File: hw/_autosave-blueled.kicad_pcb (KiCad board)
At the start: 2 copper layers, 24.1 x 54.6 mm, 18 parts, among them J1 Barrel_Jack, J2 Screw_Terminal_01x03, J3 ICSP, U1 ATmega328P-AU, U3 LM1117-3.3, X1 RESON-MURATA-CSTCE

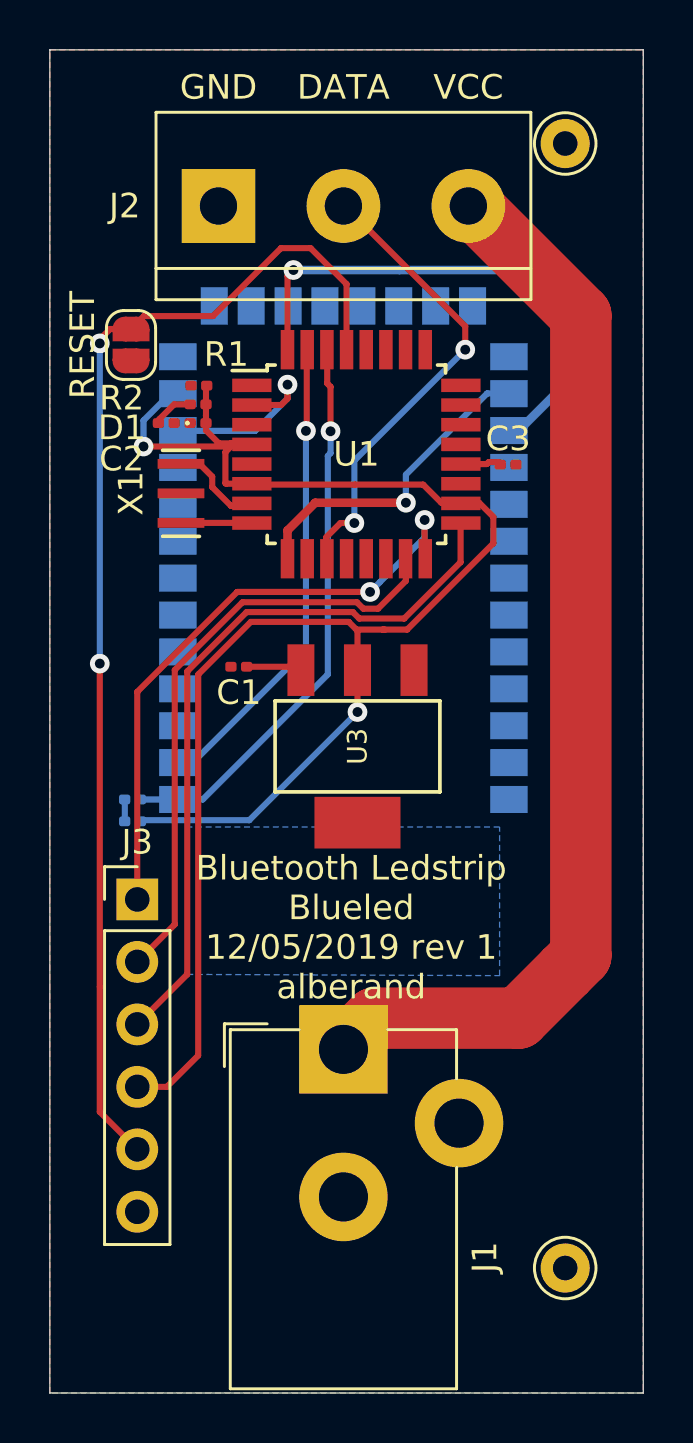
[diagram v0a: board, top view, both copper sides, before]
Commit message: hw: Mainly refactoring + add switch to the schematics
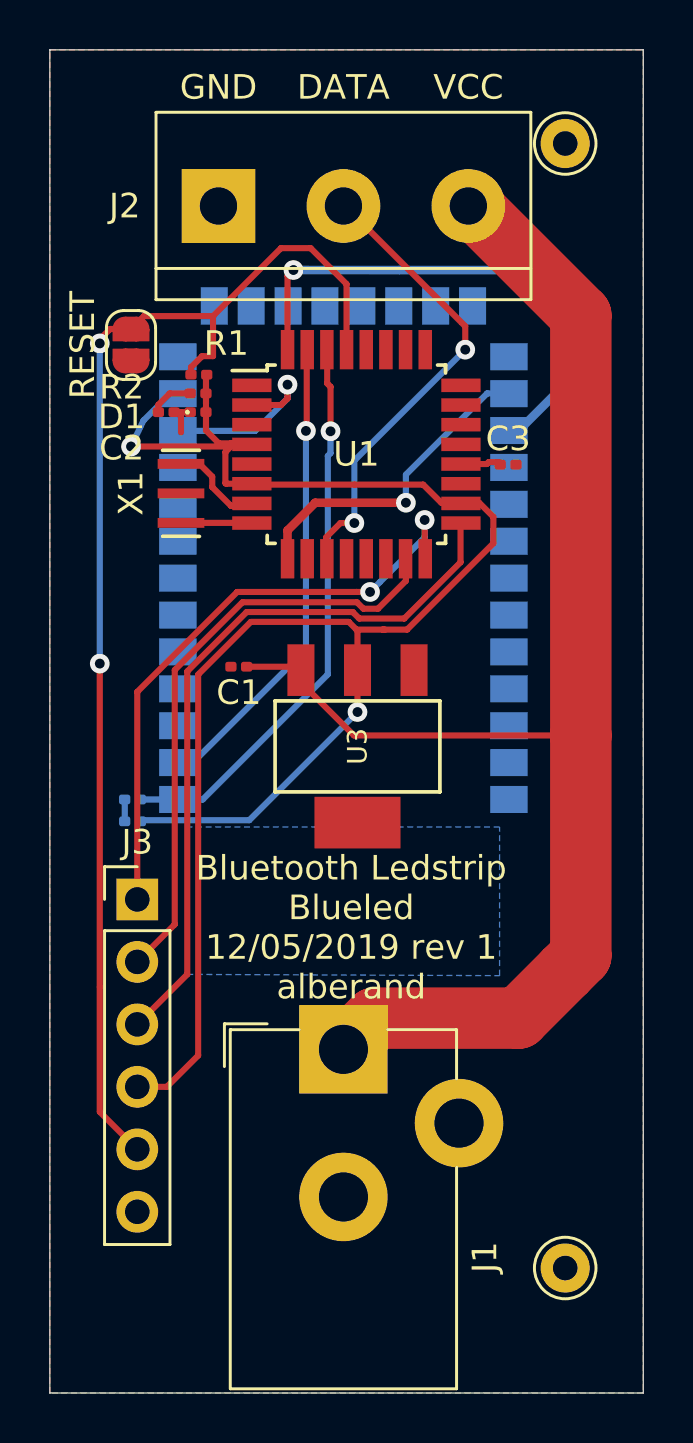
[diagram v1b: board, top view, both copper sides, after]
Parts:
- moved C2 0.44 mm to (147.0, 112.5)
- moved D1 0.44 mm to (145.7, 112.5)
- moved R1 0.44 mm to (147.0, 111.0)
- moved R2 0.44 mm to (147.0, 111.8)
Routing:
- net VIN: track 45.9 -> 58.2 mm
- net RESET: track 48.1 -> 51.2 mm
- net GND: track 0.00 -> 1.42 mm
- net +3V3: track 69.3 -> 70.3 mm
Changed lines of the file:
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@@
     (thickness 1.6)
     (drawings 5)
-    (tracks 155)
+    (tracks 165)
     (zones 0)
     (modules 18)
@@
   )
   (module Resistor_SMD:R_0201_0603Metric (layer F.Cu)
-    (at 147 112.2045 180)
+    (at 147 111.76 180)
     (descr "Resistor SMD 0201 (0603 Metric), square (rectangular) end terminal, IPC_7351 nominal, (Body size source: https://www.vishay.com/docs/20052/crcw0201e3.pdf), generated with kicad-footprint-generator")
     (tags resistor)
@@
   )
   (module LED_SMD:LED_0201_0603Metric (layer F.Cu)
-    (at 145.705 112.9665 180)
+    (at 145.705 112.522 180)
     (descr "LED SMD 0201 (0603 Metric), square (rectangular) end terminal, IPC_7351 nominal, (Body size source: https://www.vishay.com/docs/20052/crcw0201e3.pdf), generated with kicad-footprint-generator")
     (tags LED)
@@
   )
   (module Resistor_SMD:R_0201_0603Metric (layer F.Cu)
-    (at 147.03 111.4425 180)
+    (at 147.03 110.998 180)
     (descr "Resistor SMD 0201 (0603 Metric), square (rectangular) end terminal, IPC_7351 nominal, (Body size source: https://www.vishay.com/docs/20052/crcw0201e3.pdf), generated with kicad-footprint-generator")
     (tags resistor)
@@
   )
   (module Capacitor_SMD:C_0201_0603Metric (layer F.Cu)
-    (at 147 112.9665 180)
+    (at 147 112.522 180)
     (descr "Capacitor SMD 0201 (0603 Metric), square (rectangular) end terminal, IPC_7351 nominal, (Body size source: https://www.vishay.com/docs/20052/crcw0201e3.pdf), generated with kicad-footprint-generator")
     (tags capacitor)
@@
   (segment (start 147.32 113.2665) (end 147.8455 113.792) (width 0.25) (layer F.Cu) (net 1))
   (segment (start 147.32 112.9665) (end 147.32 113.2665) (width 0.25) (layer F.Cu) (net 1))
-  (via (at 144.78 113.919) (size 0.8) (drill 0.4) (layers F.Cu B.Cu) (net 1))
-  (segment (start 144.78 112.859998) (end 145.816498 111.8235) (width 0.25) (layer B.Cu) (net 1))
-  (segment (start 144.78 113.919) (end 144.78 112.859998) (width 0.25) (layer B.Cu) (net 1))
-  (segment (start 145.816498 111.8235) (end 146.1135 111.8235) (width 0.25) (layer B.Cu) (net 1))
   (segment (start 153.4795 123.011) (end 153.4795 124.714) (width 0.25) (layer F.Cu) (net 1))
   (via (at 153.4795 124.714) (size 0.8) (drill 0.4) (layers F.Cu B.Cu) (net 1))
@@
   (segment (start 153.4795 124.714) (end 149.08091 129.11259) (width 0.25) (layer B.Cu) (net 1))
   (segment (start 144.79709 129.11259) (end 144.78 129.0955) (width 0.25) (layer B.Cu) (net 1))
-  (segment (start 144.78 113.919) (end 148.209 113.919) (width 0.25) (layer F.Cu) (net 1))
-  (segment (start 148.209 113.919) (end 148.336 113.792) (width 0.25) (layer F.Cu) (net 1))
   (segment (start 147.8455 113.792) (end 148.336 113.792) (width 0.25) (layer F.Cu) (net 1))
   (segment (start 148.336 113.792) (end 148.463 113.792) (width 0.25) (layer F.Cu) (net 1))
+  (segment (start 148.209 113.919) (end 148.336 113.792) (width 0.25) (layer F.Cu) (net 1))
+  (segment (start 144.272 113.919) (end 144.78 112.859998) (width 0.25) (layer B.Cu) (net 1))
+  (via (at 144.272 113.919) (size 0.8) (drill 0.4) (layers F.Cu B.Cu) (net 1))
+  (segment (start 144.78 112.859998) (end 145.816498 111.8235) (width 0.25) (layer B.Cu) (net 1))
+  (segment (start 145.816498 111.8235) (end 146.1135 111.8235) (width 0.25) (layer B.Cu) (net 1))
+  (segment (start 144.272 113.919) (end 148.209 113.919) (width 0.25) (layer F.Cu) (net 1))
+  (segment (start 147.32 111.506) (end 147.32 111.0615) (width 0.25) (layer F.Cu) (net 1))
   (segment (start 158.7348 114.632) (end 158.8128 114.554) (width 0.25) (layer F.Cu) (net 2))
   (segment (start 157.6848 114.632) (end 158.7348 114.632) (width 0.25) (layer F.Cu) (net 2))
   (segment (start 158.8128 114.554) (end 159.258 114.554) (width 0.25) (layer F.Cu) (net 2))
-  (segment (start 146.026654 112.2045) (end 145.415 112.816154) (width 0.25) (layer F.Cu) (net 3))
-  (segment (start 146.68 112.2045) (end 146.026654 112.2045) (width 0.25) (layer F.Cu) (net 3))
-  (segment (start 145.415 112.816154) (end 145.415 112.903) (width 0.25) (layer F.Cu) (net 3))
+  (segment (start 145.385 112.222) (end 145.847 111.76) (width 0.25) (layer F.Cu) (net 3))
+  (segment (start 145.385 112.522) (end 145.385 112.222) (width 0.25) (layer F.Cu) (net 3))
+  (segment (start 145.847 111.76) (end 146.685 111.76) (width 0.25) (layer F.Cu) (net 3))
   (via (at 157.861 109.982) (size 0.8) (drill 0.4) (layers F.Cu B.Cu) (net 4))
   (via (at 153.3525 117.0305) (size 0.8) (drill 0.4) (layers F.Cu B.Cu) (net 4))
@@
   (segment (start 150.372885 112.232) (end 150.6348 111.970085) (width 0.25) (layer F.Cu) (net 21))
   (segment (start 149.1848 112.232) (end 150.372885 112.232) (width 0.25) (layer F.Cu) (net 21))
+  (segment (start 146.025 112.522) (end 146.304 112.522) (width 0.25) (layer F.Cu) (net 45))
+  (segment (start 146.304 112.522) (end 146.304 113.3475) (width 0.25) (layer F.Cu) (net 45))
+  (segment (start 146.304 112.522) (end 146.6215 112.522) (width 0.25) (layer F.Cu) (net 45))
   (segment (start 148.9735 122.8725) (end 150.8125 122.8725) (width 0.25) (layer F.Cu) (net 46))
-  (segment (start 151.1795 123.011) (end 151.1795 123.511) (width 0.35) (layer F.Cu) (net 46))
   (segment (start 152.908 138.43) (end 154.178 137.16) (width 2.5) (layer F.Cu) (net 46))
   (segment (start 154.178 137.16) (end 160.02 137.16) (width 2.5) (layer F.Cu) (net 46))
   (segment (start 160.02 137.16) (end 161.925 135.255) (width 2.5) (layer F.Cu) (net 46))
   (segment (start 161.925 135.255) (end 162.56 134.62) (width 2.5) (layer F.Cu) (net 46))
-  (segment (start 162.56 134.62) (end 162.56 108.585) (width 2.5) (layer F.Cu) (net 46))
   (segment (start 162.56 108.585) (end 158.115 104.14) (width 2.5) (layer F.Cu) (net 46))
+  (segment (start 153.335 125.6665) (end 162.56 125.6665) (width 0.25) (layer F.Cu) (net 46))
+  (segment (start 151.1795 123.511) (end 153.335 125.6665) (width 0.25) (layer F.Cu) (net 46))
+  (segment (start 162.56 134.62) (end 162.56 125.6665) (width 2.5) (layer F.Cu) (net 46))
+  (segment (start 151.1795 123.011) (end 151.1795 123.511) (width 0.25) (layer F.Cu) (net 46))
+  (segment (start 162.56 125.6665) (end 162.56 108.585) (width 2.5) (layer F.Cu) (net 46))
   (segment (start 144.013 128.27) (end 144.018 128.27) (width 0.25) (layer B.Cu) (net 47))
   (segment (start 144.018 129.0955) (end 144.018 128.27) (width 0.25) (layer B.Cu) (net 47))
@@
   (segment (start 143.002 109.728) (end 143.002 122.7455) (width 0.25) (layer B.Cu) (net 49))
   (via (at 143.002 122.7455) (size 0.8) (drill 0.4) (layers F.Cu B.Cu) (net 49))
+  (segment (start 147.605774 110.246726) (end 147.605774 108.616726) (width 0.25) (layer F.Cu) (net 49))
+  (segment (start 147.161274 110.246726) (end 147.605774 110.246726) (width 0.25) (layer F.Cu) (net 49))
+  (segment (start 146.71 110.698) (end 147.161274 110.246726) (width 0.25) (layer F.Cu) (net 49))
+  (segment (start 146.71 110.998) (end 146.71 110.698) (width 0.25) (layer F.Cu) (net 49))
   (segment (start 153.289001 120.649999) (end 153.552012 120.91301) (width 0.25) (layer F.Cu) (net 50))
   (segment (start 157.6705 118.6238) (end 157.6705 117.094) (width 0.25) (layer F.Cu) (net 50))
@@
   (segment (start 144.526 137.414) (end 146.558 135.382) (width 0.25) (layer F.Cu) (net 50))
   (segment (start 153.552012 120.91301) (end 155.38129 120.91301) (width 0.25) (layer F.Cu) (net 50))
-  (segment (start 153.416 119.888) (end 153.416 119.888) (width 0.25) (layer B.Cu) (net 51))
   (via (at 156.21 116.9054) (size 0.8) (drill 0.4) (layers F.Cu B.Cu) (net 51))
   (segment (start 156.21 116.9054) (end 156.21 118.11) (width 0.25) (layer F.Cu) (net 51))
